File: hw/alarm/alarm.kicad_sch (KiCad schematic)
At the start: 71 parts, among them IC1 SHT40-BD1B-R2, IC2 MAX31328NELB+, IC3 PEC11S-929K-S0015, J1 FFC2B35-24-T, J2 975, J3 M20-7920642R, J4 SM04B-SRSS-TB_LF__SN__P_, Q1 Si1308EDL-T1-GE3, Q2 DMG2305UX-7, Q3 DMG2305UX-7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

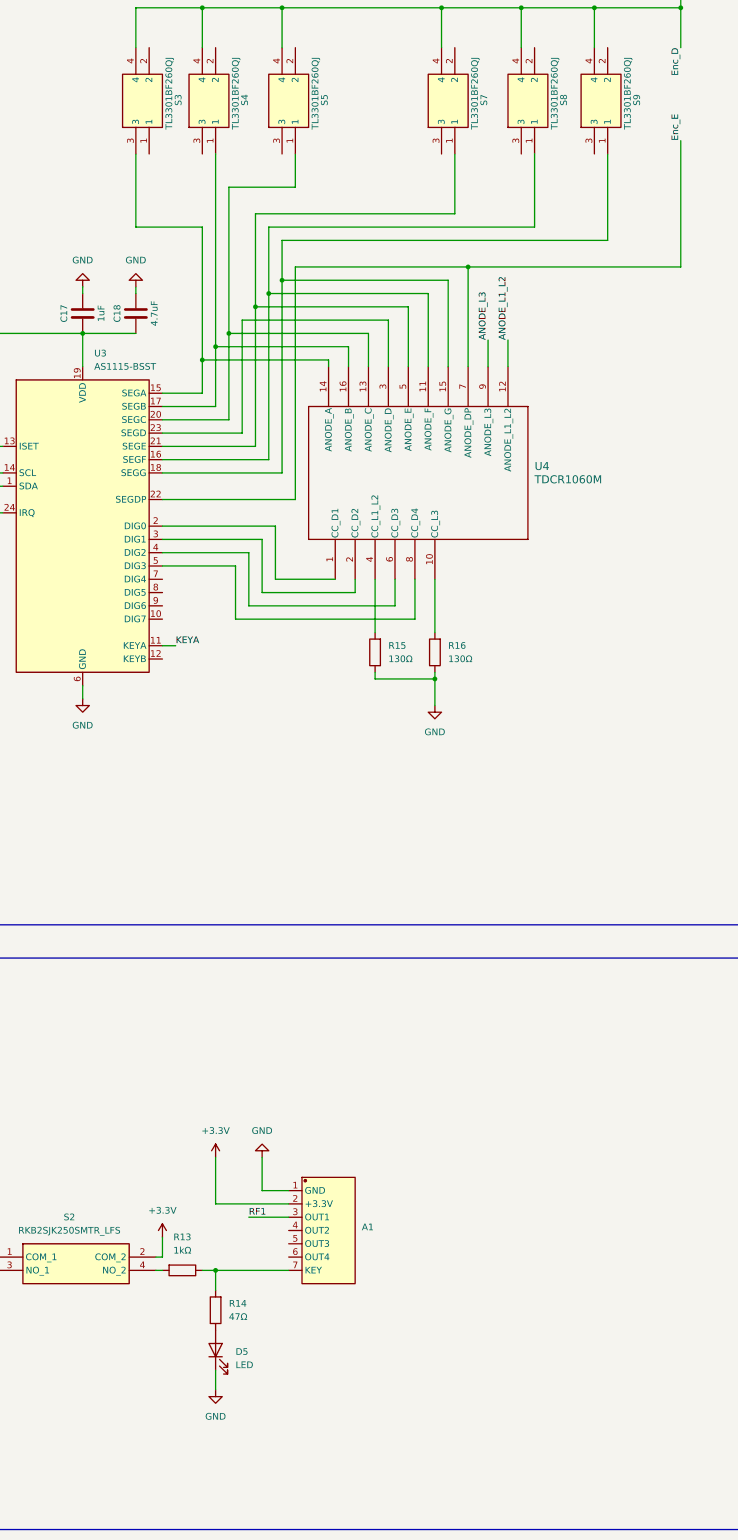
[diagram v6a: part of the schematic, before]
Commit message: Add front plate
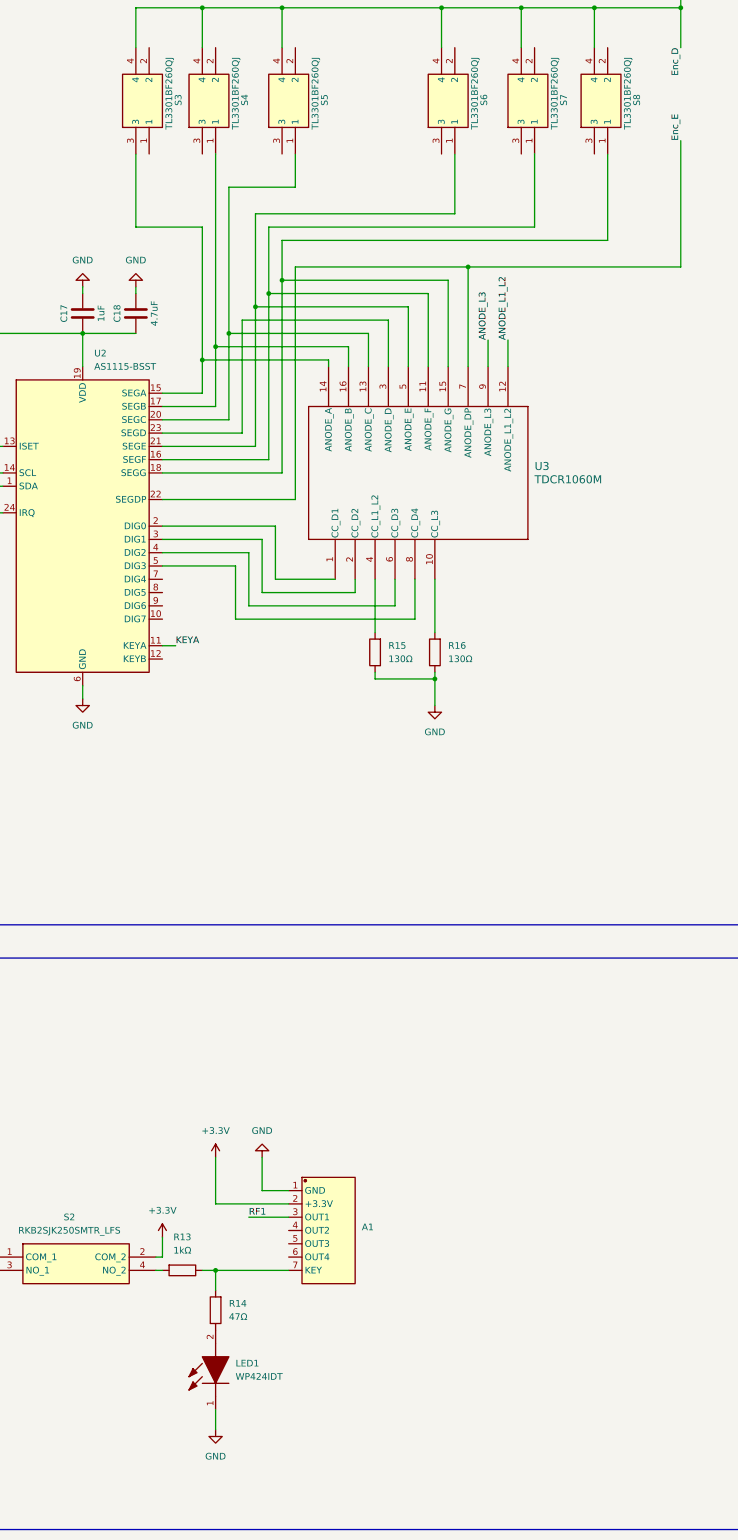
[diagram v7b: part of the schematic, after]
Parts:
- removed D5: LED, SamacSys_Parts:WP710A10LID, symbol Device:LED
- added LED1: WP424IDT, WP424IDT, symbol SamacSys_Parts:WP424IDT
- IC3: LCSC Part # (none) -> C5362681
- S3, S4, S5: LCSC Part # (none) -> C2886846
- S6: renamed from S7; LCSC Part # (none) -> C2886846
- S7: renamed from S8; LCSC Part # (none) -> C2886846
- S8: renamed from S9; LCSC Part # (none) -> C2886846
- renumbered U3 to U2, U4 to U3
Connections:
- net GND: now also LED1.1 (K)
- net at R14.1: now also LED1.2 (A)

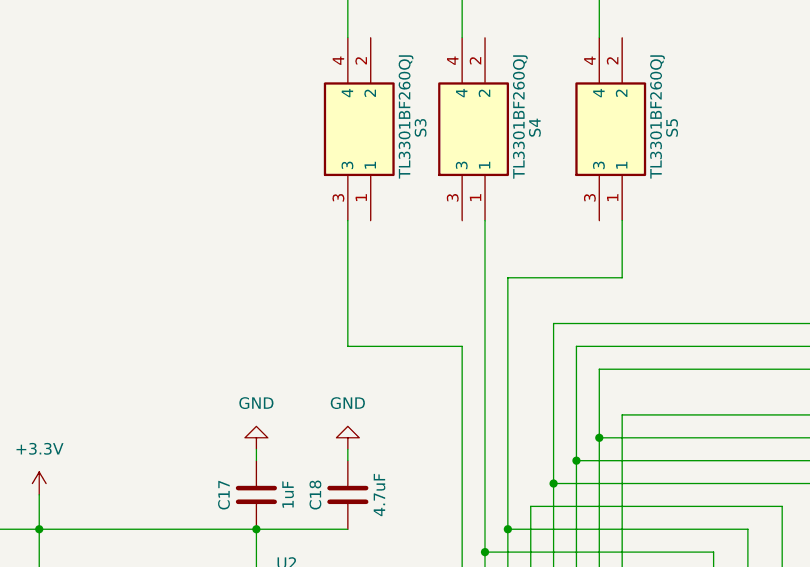
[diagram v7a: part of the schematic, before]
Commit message: Fix S3 wiring mistake and update library paths
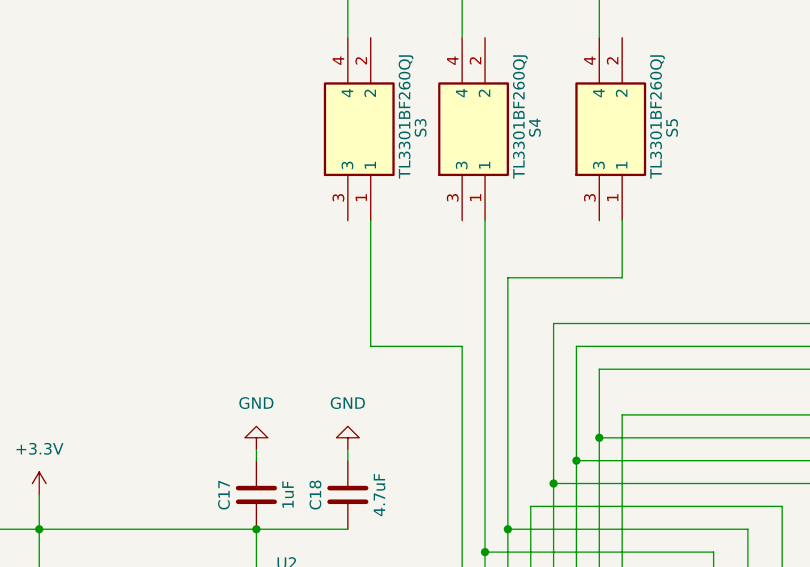
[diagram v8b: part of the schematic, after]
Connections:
- net at U2.15 (SEGA), U3.14 (ANODE_A): now also S3.1; no longer S3.3
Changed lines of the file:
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@@
-	(wire
-		(pts
-			(xy 447.04 106.68) (xy 447.04 120.65)
-		)
-		(stroke
-			(width 0)
-			(type default)
-		)
-	)
 	(wire
 		(pts
@@
 	(wire
 		(pts
-			(xy 447.04 120.65) (xy 459.74 120.65)
-		)
-		(stroke
-			(width 0)
-			(type default)
-		)
-	)
-	(wire
-		(pts
 			(xy 289.56 199.39) (xy 289.56 190.5)
 		)
@@
 	(wire
 		(pts
+			(xy 449.58 120.65) (xy 459.74 120.65)
+		)
+		(stroke
+			(width 0)
+			(type default)
+		)
+	)
+	(wire
+		(pts
 			(xy 167.64 316.23) (xy 167.64 318.77)
 		)
@@
 		)
 		(stroke
+			(width 0)
+			(type default)
+		)
+	)
+	(wire
+		(pts
+			(xy 449.58 106.68) (xy 449.58 120.65)
+		)
+		(stroke
